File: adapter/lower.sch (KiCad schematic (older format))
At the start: 13 parts, among them J1 MALE, J2 FEMALE, J3 STANDOFF, J4 STANDOFF, J5 STANDOFF, J6 USB_C_Receptacle_USB2.0, J7 DTR, U1 FT232RL

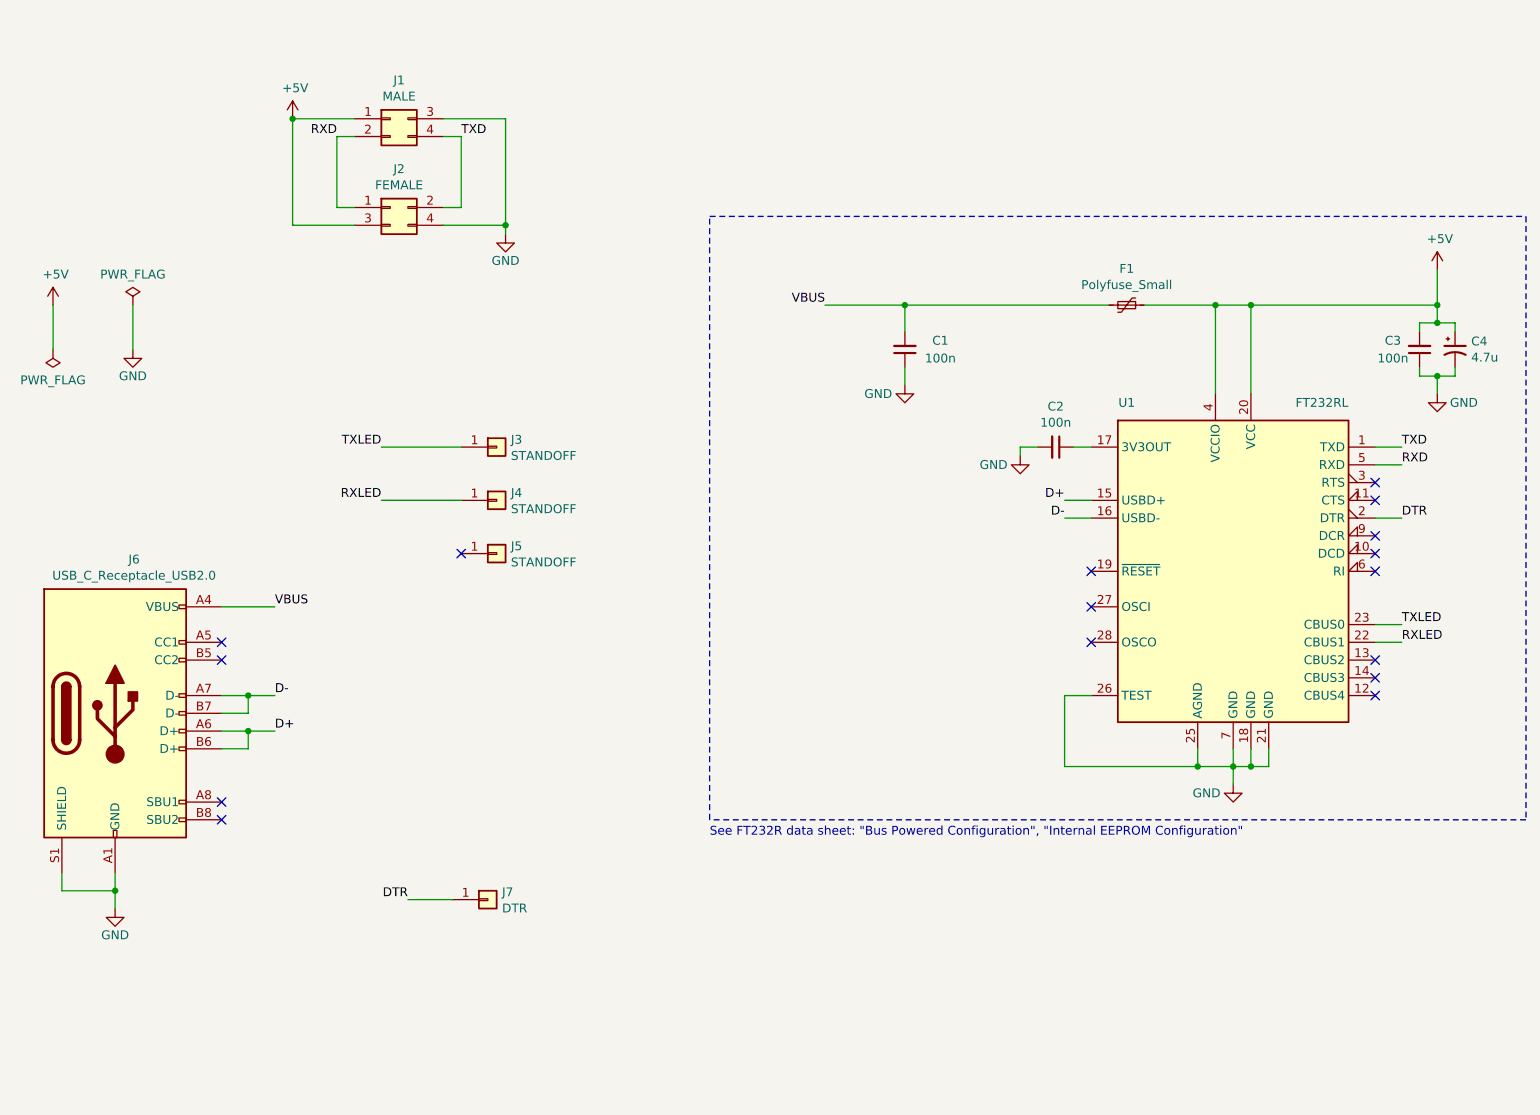
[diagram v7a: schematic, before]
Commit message: Use different power net names for lower board
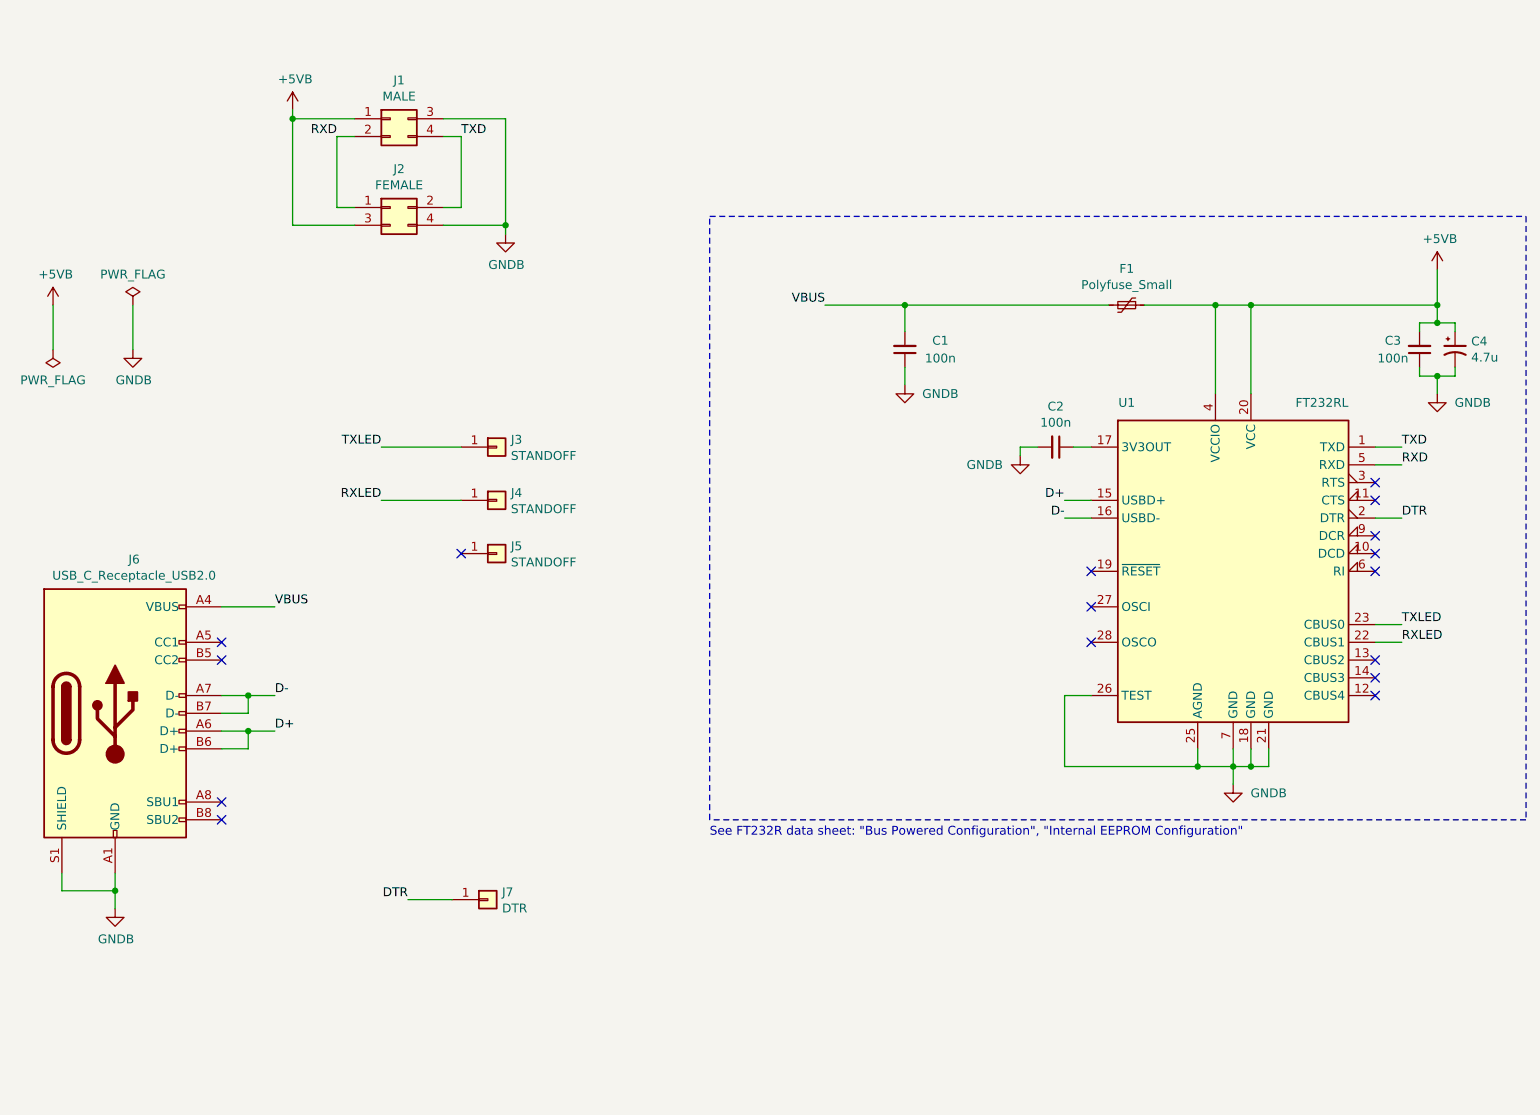
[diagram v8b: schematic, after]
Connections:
- net +5V renamed +5VB
- net GND renamed GNDB
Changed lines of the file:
@@
 Wire Wire Line
 	6950 3000 7050 3000
-$Comp
-L power:GND #PWR0101
-U 1 1 5FA70352
-P 6650 3050
-F 0 "#PWR0101" H 6650 2800 50  0001 C CNN
-F 1 "GND" H 6500 3000 50  0000 C CNN
-F 2 "" H 6650 3050 50  0001 C CNN
-F 3 "" H 6650 3050 50  0001 C CNN
-	1    6650 3050
-	1    0    0    -1
-$EndComp
 Wire Wire Line
 	6750 3000 6650 3000
 Wire Wire Line
 	6650 3000 6650 3050
-$Comp
-L power:GND #PWR0102
-U 1 1 5FA70810
-P 7850 4900
-F 0 "#PWR0102" H 7850 4650 50  0001 C CNN
-F 1 "GND" H 7700 4850 50  0000 C CNN
-F 2 "" H 7850 4900 50  0001 C CNN
-F 3 "" H 7850 4900 50  0001 C CNN
-	1    7850 4900
-	1    0    0    -1
-$EndComp
 Wire Wire Line
 	6900 4400 6900 4800
@@
 Wire Wire Line
 	6000 2200 7150 2200
-$Comp
-L power:GND #PWR0103
-U 1 1 5FA775C0
-P 6000 2650
-F 0 "#PWR0103" H 6000 2400 50  0001 C CNN
-F 1 "GND" H 5850 2600 50  0000 C CNN
-F 2 "" H 6000 2650 50  0001 C CNN
-F 3 "" H 6000 2650 50  0001 C CNN
-	1    6000 2650
-	1    0    0    -1
-$EndComp
 Wire Wire Line
 	7950 2200 9000 2200
@@
 Wire Wire Line
 	9000 2600 9100 2600
-$Comp
-L power:GND #PWR0104
-U 1 1 5FA7B81C
-P 9000 2700
-F 0 "#PWR0104" H 9000 2450 50  0001 C CNN
-F 1 "GND" H 9150 2650 50  0000 C CNN
-F 2 "" H 9000 2700 50  0001 C CNN
-F 3 "" H 9000 2700 50  0001 C CNN
-	1    9000 2700
-	1    0    0    -1
-$EndComp
 Wire Wire Line
 	8650 3400 8800 3400
@@
 Wire Wire Line
 	3400 1250 3500 1250
-$Comp
-L power:+5V #PWR0105
-U 1 1 5FA8B0B1
-P 2550 1150
-F 0 "#PWR0105" H 2550 1000 50  0001 C CNN
-F 1 "+5V" H 2565 1323 50  0000 C CNN
-F 2 "" H 2550 1150 50  0001 C CNN
-F 3 "" H 2550 1150 50  0001 C CNN
-	1    2550 1150
-	1    0    0    -1
-$EndComp
-$Comp
-L power:GND #PWR0106
-U 1 1 5FA8B1B4
-P 3750 1800
-F 0 "#PWR0106" H 3750 1550 50  0001 C CNN
-F 1 "GND" H 3750 1650 50  0000 C CNN
-F 2 "" H 3750 1800 50  0001 C CNN
-F 3 "" H 3750 1800 50  0001 C CNN
-	1    3750 1800
-	1    0    0    -1
-$EndComp
 Text Label 3500 1250 0    50   ~ 0
 TXD
 Text Label 2800 1250 2    50   ~ 0
 RXD
-$Comp
-L power:+5V #PWR0107
-U 1 1 5FA78C59
-P 9000 2000
-F 0 "#PWR0107" H 9000 1850 50  0001 C CNN
-F 1 "+5V" H 9015 2173 50  0000 C CNN
-F 2 "" H 9000 2000 50  0001 C CNN
-F 3 "" H 9000 2000 50  0001 C CNN
-	1    9000 2000
-	1    0    0    -1
-$EndComp
 Wire Wire Line
 	8650 4000 8800 4000
@@
 	3750 1150 3750 1750
 Connection ~ 3750 1750
-Connection ~ 2550 1150
 Wire Wire Line
 	2900 1250 2800 1250
@@
 Text Label 2450 4400 0    50   ~ 0
 D-
-$Comp
-L power:GND #PWR0112
-U 1 1 5FBCF965
-P 1550 5600
-F 0 "#PWR0112" H 1550 5350 50  0001 C CNN
-F 1 "GND" H 1550 5450 50  0000 C CNN
-F 2 "" H 1550 5600 50  0001 C CNN
-F 3 "" H 1550 5600 50  0001 C CNN
-	1    1550 5600
-	1    0    0    -1
-$EndComp
 Wire Wire Line
 	1250 5400 1250 5500
@@
 NoConn ~ 2150 5000
 NoConn ~ 2150 5100
-$Comp
-L power:+5V #PWR0113
-U 1 1 5FB6B75B
-P 1200 2200
-F 0 "#PWR0113" H 1200 2050 50  0001 C CNN
-F 1 "+5V" H 1215 2373 50  0000 C CNN
-F 2 "" H 1200 2200 50  0001 C CNN
-F 3 "" H 1200 2200 50  0001 C CNN
-	1    1200 2200
-	1    0    0    -1
-$EndComp
-$Comp
-L power:GND #PWR0114
-U 1 1 5FB6B9B3
-P 1650 2450
-F 0 "#PWR0114" H 1650 2200 50  0001 C CNN
-F 1 "GND" H 1650 2300 50  0000 C CNN
-F 2 "" H 1650 2450 50  0001 C CNN
-F 3 "" H 1650 2450 50  0001 C CNN
-	1    1650 2450
-	1    0    0    -1
-$EndComp
 $Comp
 L power:PWR_FLAG #FLG0101
@@
 $EndComp
 Wire Wire Line
-	1200 2200 1200 2450
-Wire Wire Line
 	1650 2200 1650 2450
 $Comp
@@
 	1    0    0    -1
 $EndComp
+$Comp
+L node:+5VB #PWR?
+U 1 1 5FBBDFD6
+P 2550 1100
+F 0 "#PWR?" H 2550 950 50  0001 C CNN
+F 1 "+5VB" H 2565 1273 50  0000 C CNN
+F 2 "" H 2550 1100 50  0001 C CNN
+F 3 "" H 2550 1100 50  0001 C CNN
+	1    2550 1100
+	1    0    0    -1
+$EndComp
+Wire Wire Line
+	2550 1100 2550 1150
+Connection ~ 2550 1150
+Wire Wire Line
+	1200 2200 1200 2450
+$Comp
+L node:+5VB #PWR?
+U 1 1 5FBC099F
+P 1200 2200
+F 0 "#PWR?" H 1200 2050 50  0001 C CNN
+F 1 "+5VB" H 1215 2373 50  0000 C CNN
+F 2 "" H 1200 2200 50  0001 C CNN
+F 3 "" H 1200 2200 50  0001 C CNN
+	1    1200 2200
+	1    0    0    -1
+$EndComp
+$Comp
+L node:+5VB #PWR?
+U 1 1 5FBC0B3A
+P 9000 2000
+F 0 "#PWR?" H 9000 1850 50  0001 C CNN
+F 1 "+5VB" H 9015 2173 50  0000 C CNN
+F 2 "" H 9000 2000 50  0001 C CNN
+F 3 "" H 9000 2000 50  0001 C CNN
+	1    9000 2000
+	1    0    0    -1
+$EndComp
+$Comp
+L node:GNDB #PWR?
+U 1 1 5FBC113D
+P 1550 5600
+F 0 "#PWR?" H 1550 5350 50  0001 C CNN
+F 1 "GNDB" H 1555 5427 50  0000 C CNN
+F 2 "" H 1550 5600 50  0001 C CNN
+F 3 "" H 1550 5600 50  0001 C CNN
+	1    1550 5600
+	1    0    0    -1
+$EndComp
+$Comp
+L node:GNDB #PWR?
+U 1 1 5FBC146F
+P 1650 2450
+F 0 "#PWR?" H 1650 2200 50  0001 C CNN
+F 1 "GNDB" H 1655 2277 50  0000 C CNN
+F 2 "" H 1650 2450 50  0001 C CNN
+F 3 "" H 1650 2450 50  0001 C CNN
+	1    1650 2450
+	1    0    0    -1
+$EndComp
+$Comp
+L node:GNDB #PWR?
+U 1 1 5FBC158B
+P 7850 4900
+F 0 "#PWR?" H 7850 4650 50  0001 C CNN
+F 1 "GNDB" H 8050 4850 50  0000 C CNN
+F 2 "" H 7850 4900 50  0001 C CNN
+F 3 "" H 7850 4900 50  0001 C CNN
+	1    7850 4900
+	1    0    0    -1
+$EndComp
+$Comp
+L node:GNDB #PWR?
+U 1 1 5FBC1AD4
+P 9000 2700
+F 0 "#PWR?" H 9000 2450 50  0001 C CNN
+F 1 "GNDB" H 9200 2650 50  0000 C CNN
+F 2 "" H 9000 2700 50  0001 C CNN
+F 3 "" H 9000 2700 50  0001 C CNN
+	1    9000 2700
+	1    0    0    -1
+$EndComp
+$Comp
+L node:GNDB #PWR?
+U 1 1 5FBC1BF2
+P 6000 2650
+F 0 "#PWR?" H 6000 2400 50  0001 C CNN
+F 1 "GNDB" H 6200 2600 50  0000 C CNN
+F 2 "" H 6000 2650 50  0001 C CNN
+F 3 "" H 6000 2650 50  0001 C CNN
+	1    6000 2650
+	1    0    0    -1
+$EndComp
+$Comp
+L node:GNDB #PWR?
+U 1 1 5FBC1D04
+P 6650 3050
+F 0 "#PWR?" H 6650 2800 50  0001 C CNN
+F 1 "GNDB" H 6450 3000 50  0000 C CNN
+F 2 "" H 6650 3050 50  0001 C CNN
+F 3 "" H 6650 3050 50  0001 C CNN
+	1    6650 3050
+	1    0    0    -1
+$EndComp
+$Comp
+L node:GNDB #PWR?
+U 1 1 5FBC21C4
+P 3750 1800
+F 0 "#PWR?" H 3750 1550 50  0001 C CNN
+F 1 "GNDB" H 3755 1627 50  0000 C CNN
+F 2 "" H 3750 1800 50  0001 C CNN
+F 3 "" H 3750 1800 50  0001 C CNN
+	1    3750 1800
+	1    0    0    -1
+$EndComp
